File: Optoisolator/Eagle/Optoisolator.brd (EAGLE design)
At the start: 59 x 45.4 mm, 18 parts

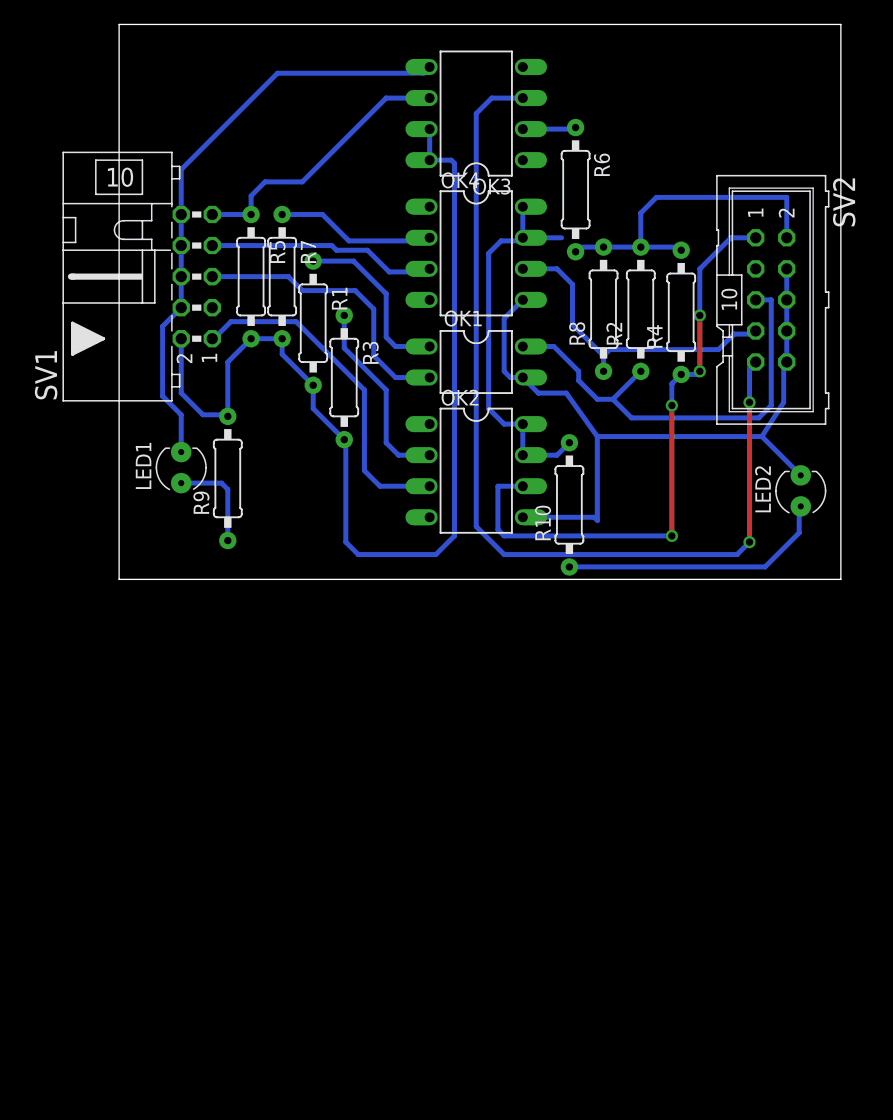
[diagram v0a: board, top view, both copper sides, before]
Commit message: Routed right-hand side of optoisolator
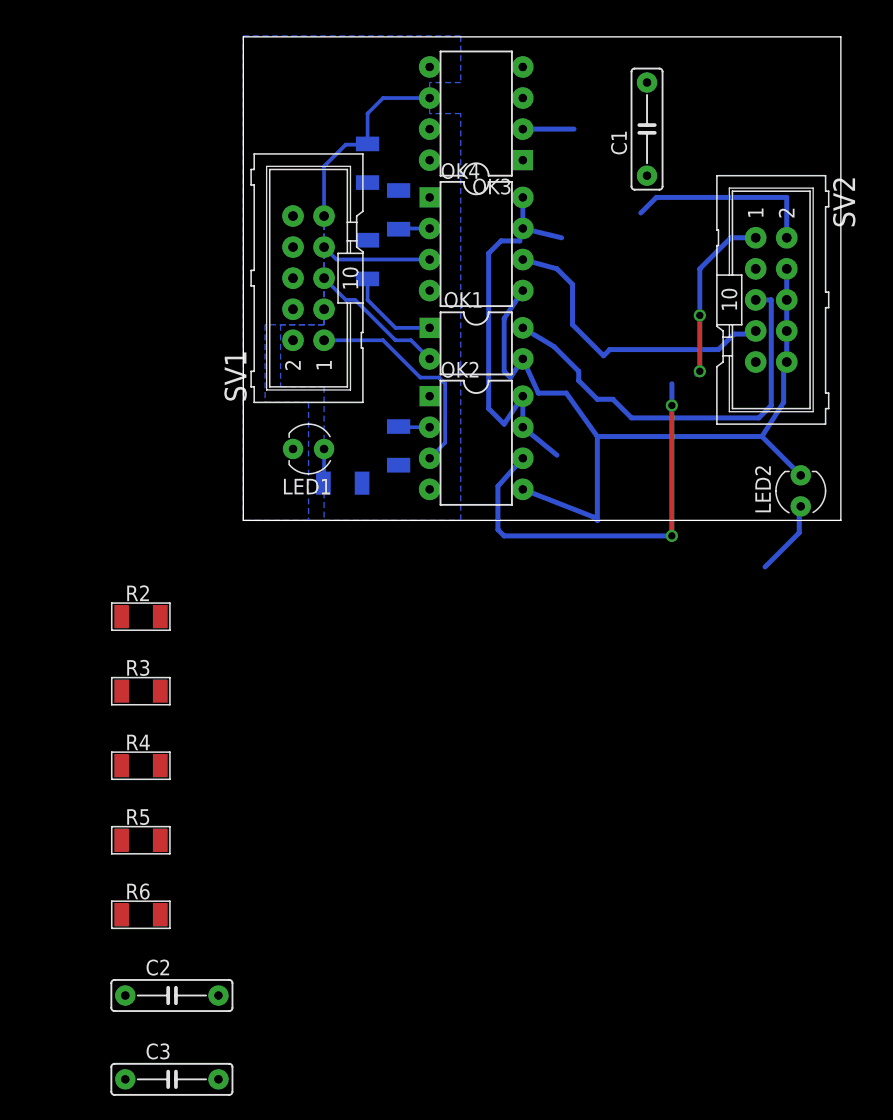
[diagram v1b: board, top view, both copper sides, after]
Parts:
- removed R10, R8, R9: 1k, Analog:0207/10
- removed R7: 240, Analog:0207/10
- added C1, C2, C3: 470n, Optoisolator:C050-025X075
- added R11, R12, R14: 240, Passive-PoE-ClassB:R1206
- added R13: 1k, Passive-PoE-ClassB:R1206
- LED1, LED2: value green -> red; device Passive.PoE.LV:LED3MM -> Optoisolator:LED3MM
- OK1: device optocoupler:DIL04 -> Optoisolator:DIL04
- OK2, OK3, OK4: device optocoupler:DIL08 -> Optoisolator:DIL08
- R1, R6: value 240 -> 510; device Analog:0207/10 -> Passive-PoE-ClassB:R1206
- R2, R5: device Analog:0207/10 -> Passive-PoE-ClassB:R1206
- R3: value 240 -> 1k; device Analog:0207/10 -> Passive-PoE-ClassB:R1206
- R4: value 1k -> 240; device Analog:0207/10 -> Passive-PoE-ClassB:R1206
- SV1: value ISP10_PROG -> ISP10_TARG; device con-ml:ML10L -> Optoisolator:ML10
- SV2: device con-ml:ML10 -> Optoisolator:ML10
- moved R6 69.2 mm to (1.78, -16.0), turned to 0 degrees
- moved R4 57.7 mm to (1.78, -3.81), turned to 0 degrees
- moved R2 48.0 mm to (1.78, 8.38), turned to 0 degrees
- moved R5 47.0 mm to (1.78, -9.91), turned to 0 degrees
- moved R3 30.6 mm to (1.78, 2.29), turned to 0 degrees
- moved R1 13.3 mm to (18.3, 19.3), flipped to the bottom, turned to 180 degrees
- moved LED1 10.5 mm to (15.5, 22.1), turned to 180 degrees
- moved SV1 9.14 mm to (15.5, 36.1)
- moved OK2 2.29 mm to (29.2, 22.6)
- moved OK1 1.52 mm to (29.2, 30.7)
- moved OK4 0.76 mm to (29.2, 38.9)
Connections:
- net GND_PROG: now also C2.2
- net GND_TARG: now also C1.2, C3.2
- net MISO_PROG: now also R13.1; no longer R5.1
- net MOSI_TARG: now also R3.1; no longer R4.1
- net N$1: now also R11.1; no longer R1.1
- net N$12: now also R4.1; no longer R6.1
- net N$2: now also R12.1; no longer R3.1
- net N$3: now also R14.1; no longer R7.1
- net N$4: now also R6.1; no longer R10.1
- net N$5: now also R1.1; no longer R9.1
- net SCK_TARG: now also R5.1; no longer R8.1
- net VCC_PROG: now also C2.1, R11.2, R12.2, R13.2, R14.2; no longer R3.2, R5.2, R7.2, R9.2
- net VCC_TARG: now also C1.1, C3.1, R3.2, R5.2; no longer R10.2, R8.2
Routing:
- net VCC_PROG: track 82.6 -> 0.00 mm
- net MISO_TARG: track 76.8 -> 0.00 mm, vias 2 -> 0
- net GND_PROG: track 48.2 -> 0.00 mm
- net N$4: track 22.2 -> 6.16 mm
- net N$2: track 15.8 -> 2.56 mm
- net !RST_PROG: track 23.4 -> 11.4 mm
- net N$3: track 13.1 -> 2.56 mm
- net MOSI_PROG: track 27.8 -> 18.0 mm
- net VCC_TARG: track 58.7 -> 49.0 mm
- net SCK_PROG: track 18.8 -> 9.06 mm
- net N$1: track 14.5 -> 7.75 mm
- net MISO_PROG: track 22.6 -> 16.5 mm
- net N$5: track 8.21 -> 2.82 mm
- net GND_TARG: track 62.0 -> 65.1 mm
- net !RST_TARG: track 36.7 -> 33.9 mm
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- added copper zone on layer 16, net GND_PROG
- added copper zone on layer 16, net VCC_PROG
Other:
- board size 59 x 45.4 mm -> 48.9 x 39.5 mm

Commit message: Routed optoisolator
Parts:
- moved C2 75.7 mm to (22.9, 50.8), turned to 90 degrees
- moved R4 60.8 mm to (35.6, 46.7), flipped to the bottom, turned to 270 degrees
- moved R5 60.6 mm to (38.1, 38.6), flipped to the bottom, turned to 90 degrees
- moved C3 59.6 mm to (35.6, 21.3), turned to 270 degrees
- moved R3 57.1 mm to (42.4, 42.4), flipped to the bottom
- moved R6 55.7 mm to (40.6, 23.9), flipped to the bottom
- moved R2 49.2 mm to (40.6, 38.6), flipped to the bottom, turned to 90 degrees
- moved C1 13.1 mm to (35.6, 37.6), turned to 270 degrees
- moved LED2 8.24 mm to (48.3, 22.1), turned to 0 degrees
- moved SV2 5.38 mm to (48.3, 36.1)
- moved R1 0.25 mm to (18.0, 19.3)
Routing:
- net GND_TARG: track 65.1 -> 0.00 mm
- net VCC_TARG: track 49.0 -> 0.00 mm
- net MISO_TARG: track 0.00 -> 33.8 mm, vias 0 -> 2
- net !RST_TARG: track 33.9 -> 20.9 mm
- net MOSI_TARG: track 47.9 -> 36.1 mm, vias 4 -> 2
- net SCK_TARG: track 24.9 -> 21.4 mm
- net N$12: track 4.19 -> 2.56 mm
- net N$4: track 6.16 -> 5.51 mm
- added copper zone on layer 16, net GND_TARG
- added copper zone on layer 16, net VCC_TARG
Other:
- board size 48.9 x 39.5 mm -> 43.5 x 40.1 mm

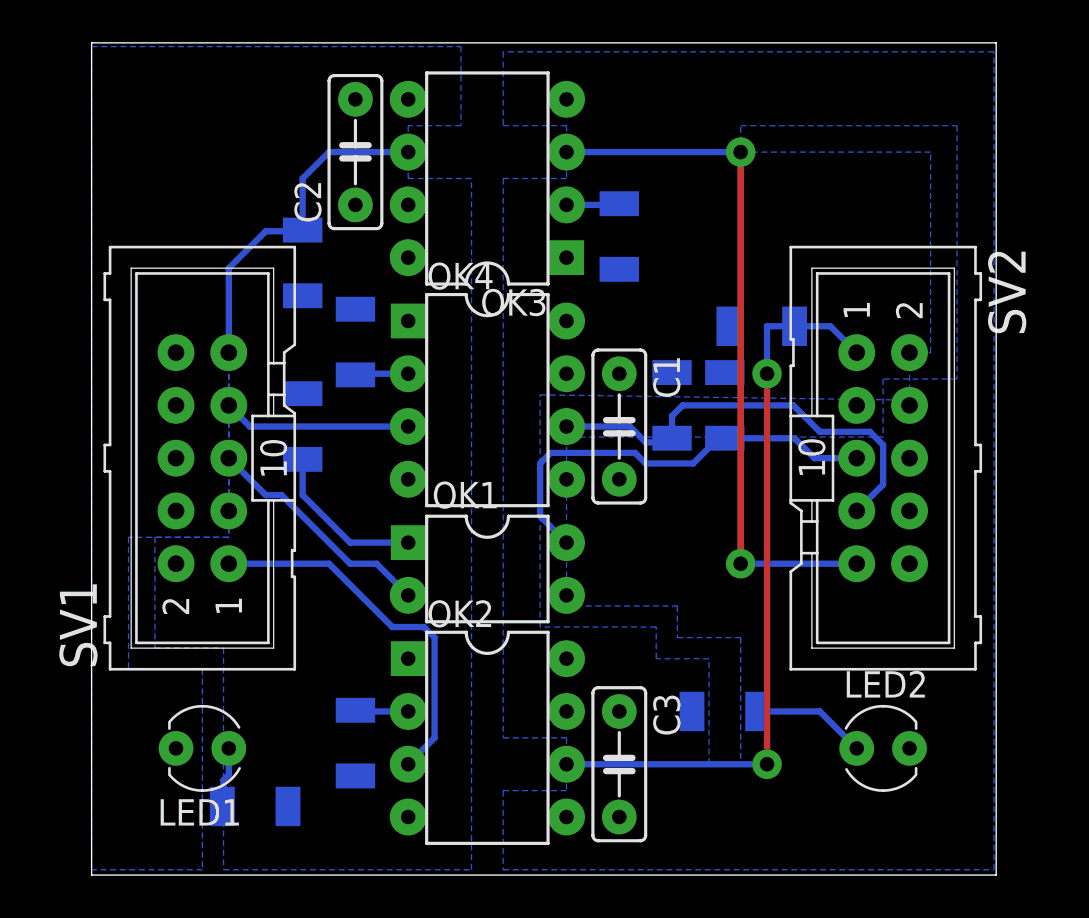
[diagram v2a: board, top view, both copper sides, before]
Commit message: Replaced through-hole bypass capacitors with smd one
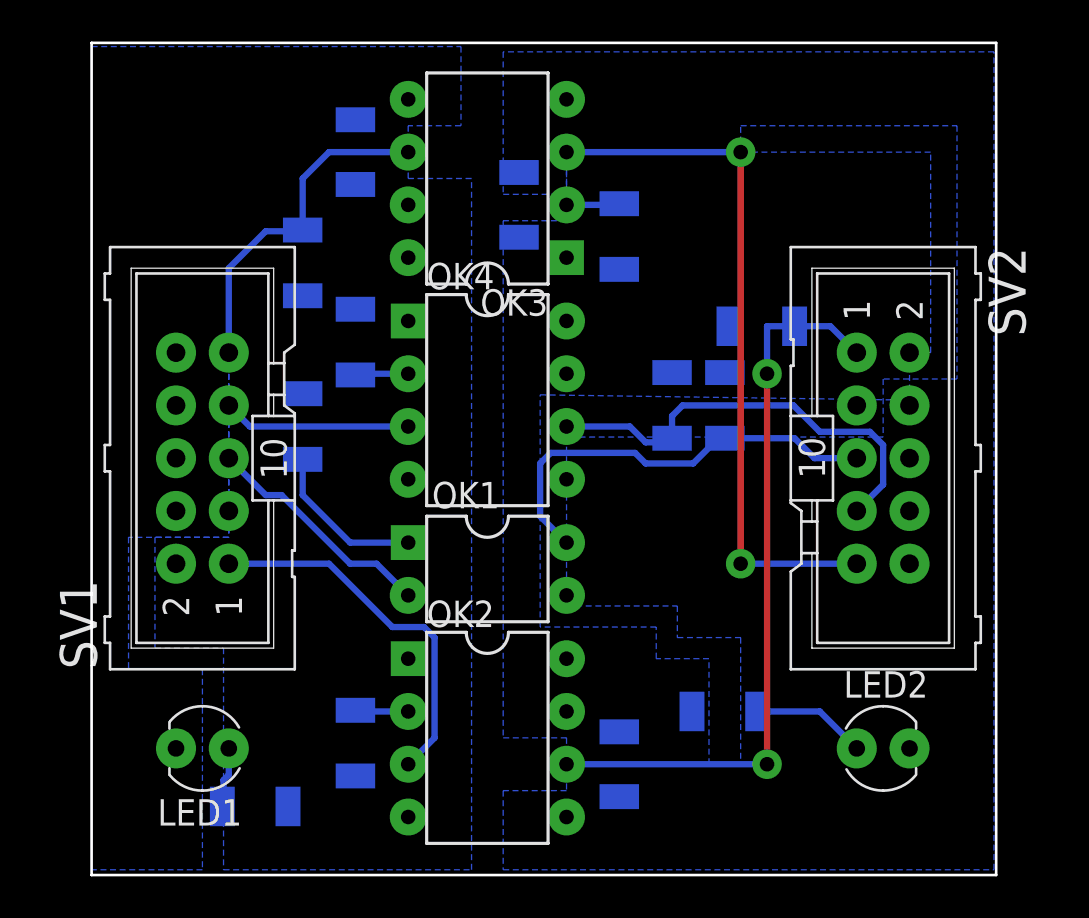
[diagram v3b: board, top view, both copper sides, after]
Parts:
- C1, C2, C3: device Optoisolator:C050-025X075 -> Passive-PoE-ClassB:C1206
- moved C1 11.7 mm to (30.7, 48.3), flipped to the bottom, turned to 90 degrees
- flipped C2 to the bottom
- flipped C3 to the bottom
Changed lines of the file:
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@@
 <board>
 <plain>
-<wire x1="10.16" y1="16.002" x2="53.701" y2="16.002" width="0" layer="20"/>
-<wire x1="53.701" y1="16.002" x2="53.701" y2="56.058" width="0" layer="20"/>
-<wire x1="53.701" y1="56.058" x2="10.16" y2="56.058" width="0" layer="20"/>
-<wire x1="10.16" y1="56.058" x2="10.16" y2="16.002" width="0" layer="20"/>
+<wire x1="10.16" y1="16.002" x2="53.701" y2="16.002" width="0.127" layer="20"/>
+<wire x1="53.701" y1="16.002" x2="53.701" y2="56.058" width="0.127" layer="20"/>
+<wire x1="53.701" y1="56.058" x2="10.16" y2="56.058" width="0.127" layer="20"/>
+<wire x1="10.16" y1="56.058" x2="10.16" y2="16.002" width="0.127" layer="20"/>
 </plain>
 <attributes>
@@
 <element name="R5" library="Passive-PoE-ClassB" package="R1206" value="1k" x="38.1" y="38.608" rot="MR90"/>
 <element name="R6" library="Passive-PoE-ClassB" package="R1206" value="510" x="40.64" y="23.876" rot="MR0"/>
-<element name="C1" library="Optoisolator" package="C050-025X075" value="470n" x="35.56" y="37.592" rot="R270"/>
-<element name="C2" library="Optoisolator" package="C050-025X075" value="470n" x="22.86" y="50.8" rot="R90"/>
-<element name="C3" library="Optoisolator" package="C050-025X075" value="470n" x="35.56" y="21.336" rot="R270"/>
+<element name="C1" library="Passive-PoE-ClassB" package="C1206" value="470n" x="30.734" y="48.26" rot="MR90"/>
+<element name="C2" library="Passive-PoE-ClassB" package="C1206" value="470n" x="22.86" y="50.8" rot="MR90"/>
+<element name="C3" library="Passive-PoE-ClassB" package="C1206" value="470n" x="35.56" y="21.336" rot="MR270"/>
 </elements>
 <signals>
@@
 <vertex x="50.546" y="50.8"/>
 <vertex x="33.02" y="50.8"/>
-<vertex x="33.02" y="49.53"/>
-<vertex x="29.972" y="49.53"/>
+<vertex x="33.02" y="47.498"/>
+<vertex x="29.972" y="47.498"/>
 <vertex x="29.972" y="22.606"/>
 <vertex x="33.02" y="22.606"/>
@@
 <vertex x="53.594" y="55.626"/>
 <vertex x="29.972" y="55.626"/>
-<vertex x="29.972" y="52.07"/>
-<vertex x="33.02" y="52.07"/>
+<vertex x="29.972" y="48.768"/>
+<vertex x="33.02" y="48.768"/>
 <vertex x="33.02" y="50.8"/>
 <vertex x="41.402" y="50.8"/>
